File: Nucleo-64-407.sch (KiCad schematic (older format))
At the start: 72 parts, among them J1 SWD, J3 USB_B_Micro, J4 Serial 0, J5 EXP1, J6 EXP2, J7 EXP3, J8 EXP4, SW1 RESET, SW2 BOOT, U1 STM32F407VETx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

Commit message: Renamed Button so it does not contain space in teh anme.
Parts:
- SW1, SW2: footprint PrntrBoardV1:Button 4x4 -> PrntrBoardV1:Button_4x4
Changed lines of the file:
@@
-EESchema Schematic File Version 4
+EESchema Schematic File Version 5
 LIBS:Nucleo-64-407-cache
 EELAYER 29 0
@@
 F 0 "SW1" H 1300 1435 50  0000 C CNN
 F 1 "RESET" H 1300 1344 50  0000 C CNN
-F 2 "PrntrBoardV1:Button 4x4" H 1300 1350 50  0001 C CNN
+F 2 "PrntrBoardV1:Button_4x4" H 1300 1350 50  0001 C CNN
 F 3 "" H 1300 1350 50  0001 C CNN
 	1    1300 1150
@@
 F 0 "SW2" H 9450 6535 50  0000 C CNN
 F 1 "BOOT" H 9450 6444 50  0000 C CNN
-F 2 "PrntrBoardV1:Button 4x4" H 9450 6450 50  0001 C CNN
+F 2 "PrntrBoardV1:Button_4x4" H 9450 6450 50  0001 C CNN
 F 3 "" H 9450 6450 50  0001 C CNN
 	1    9450 6250

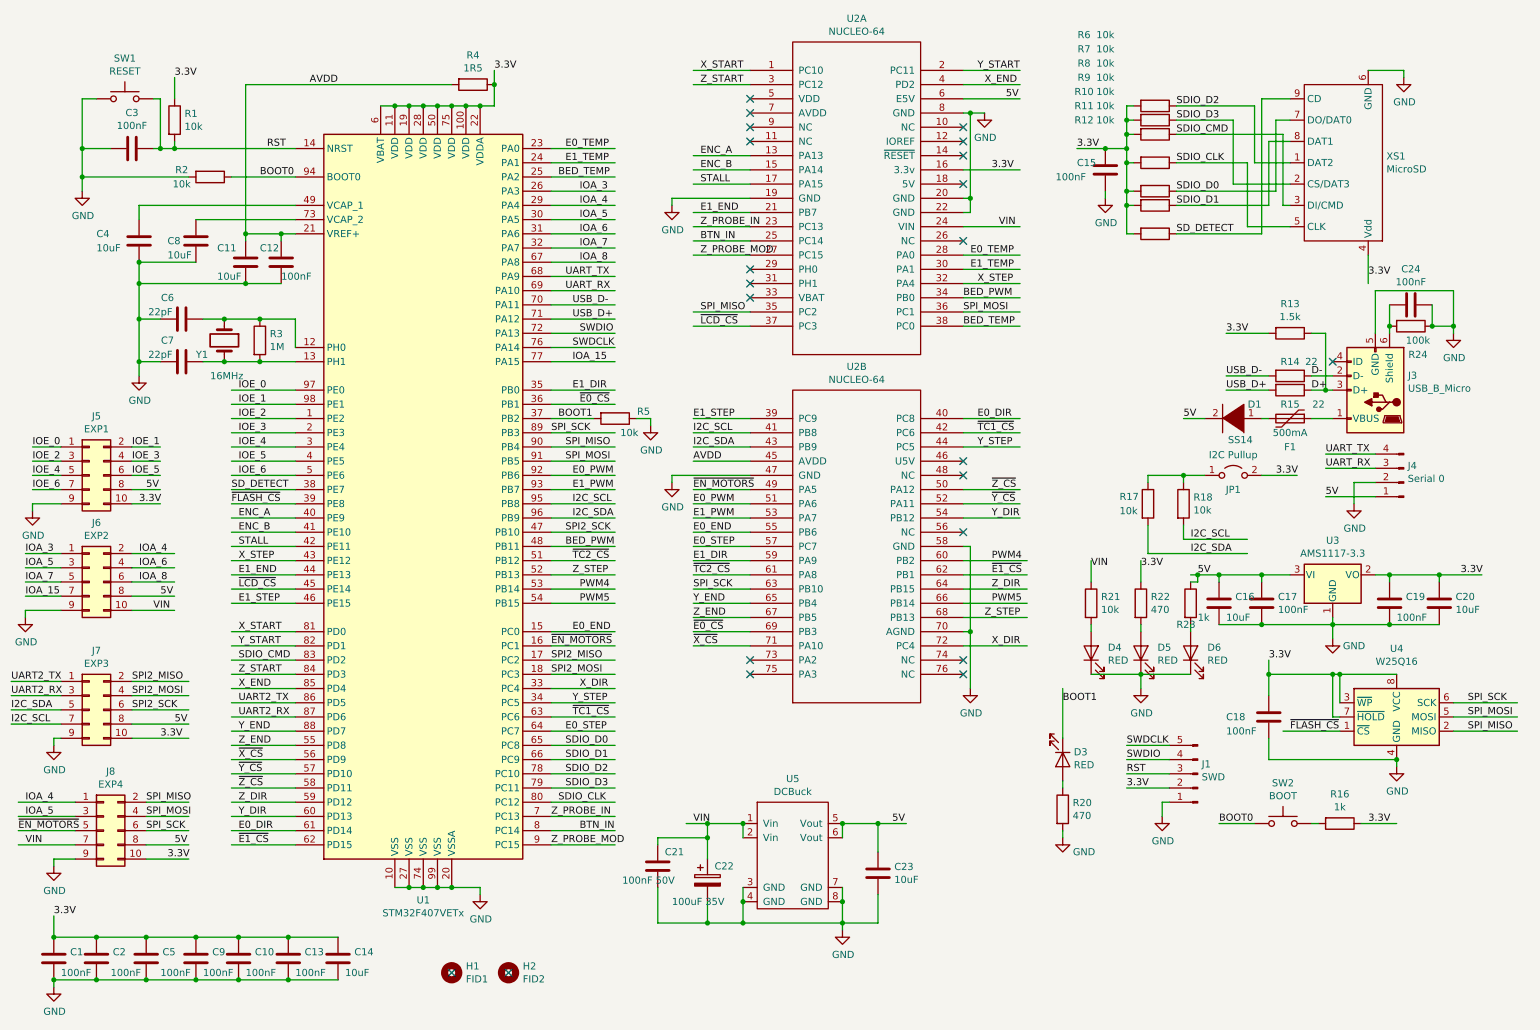
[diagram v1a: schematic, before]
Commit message: Minor updates to the nucleo-64 board. Added more signals to the extension headers. Use resistor networks. Fix diode footprint.
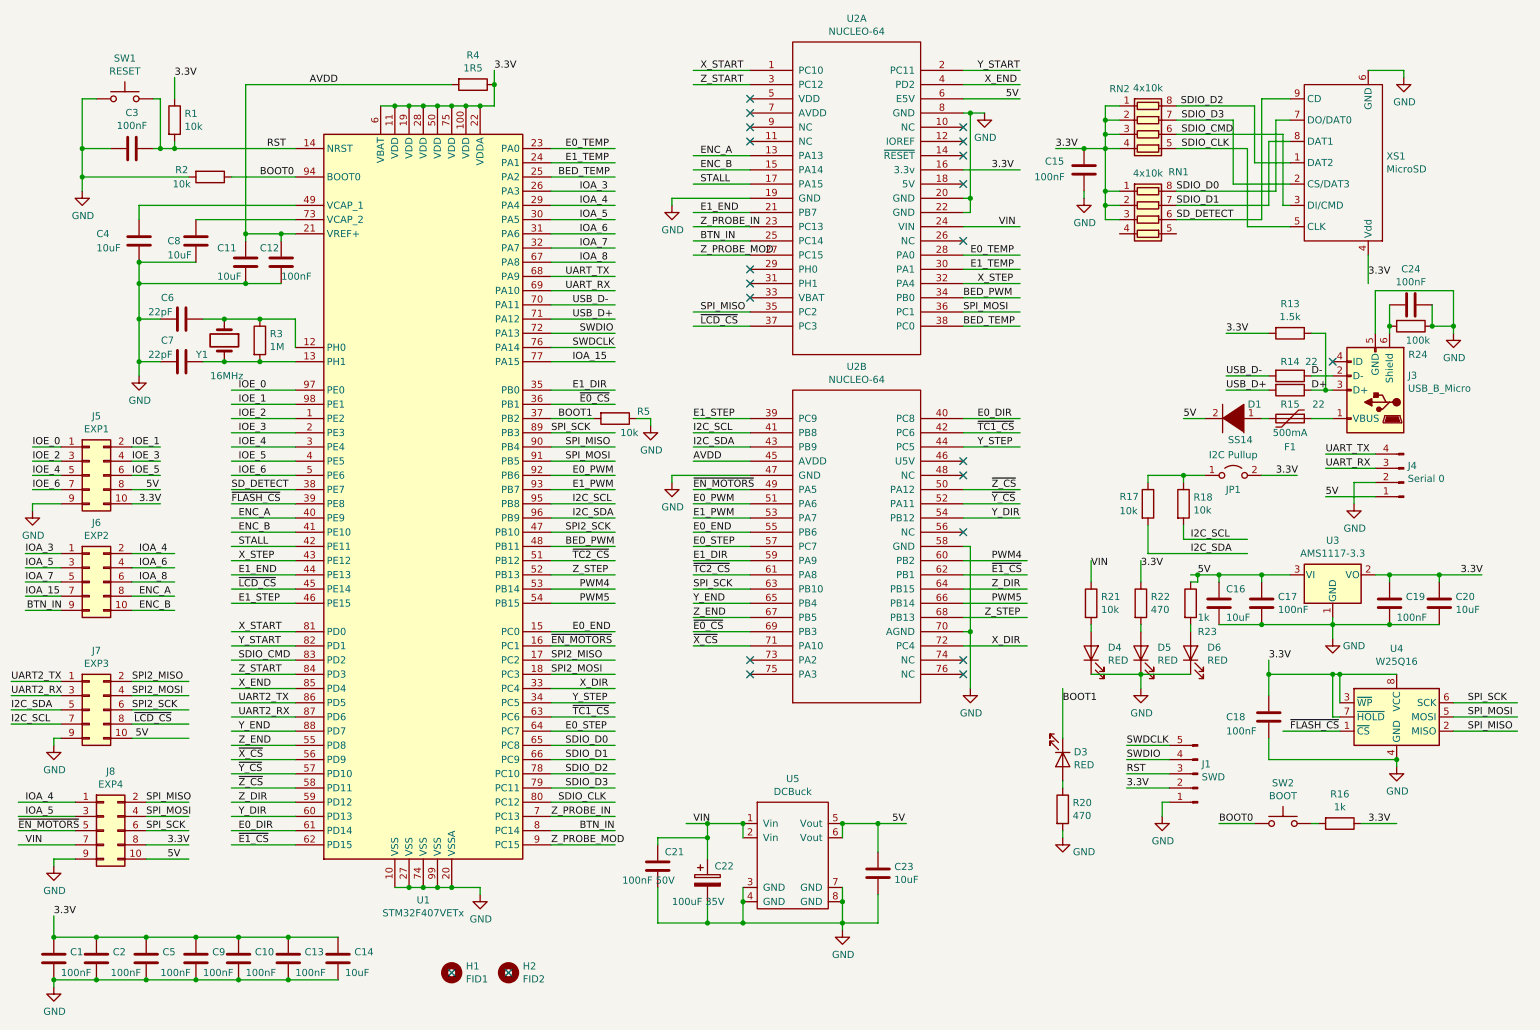
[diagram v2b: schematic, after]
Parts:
- removed R10, R11, R12, R6, R7, R8, R9: 10k, PrntrBoardV1:R_0603_1608Metric, symbol Device:R
- added RN1, RN2: 4x10k, Resistor_SMD:R_Array_Convex_4x0603, symbol Device:R_Pack04
- D1: footprint Diode_SMD:D_SOD-123F -> Diode_SMD:D_SMA
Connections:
- wire segments 410 -> 408
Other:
- moved on the sheet: C15

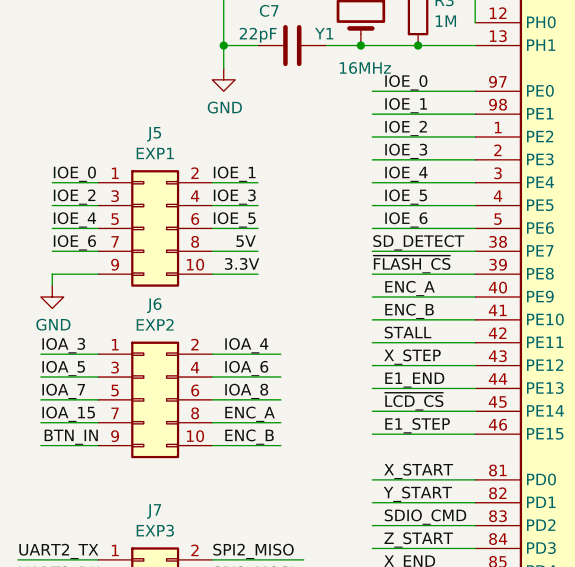
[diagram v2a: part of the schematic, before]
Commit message: Add RGB leds to IO pins.
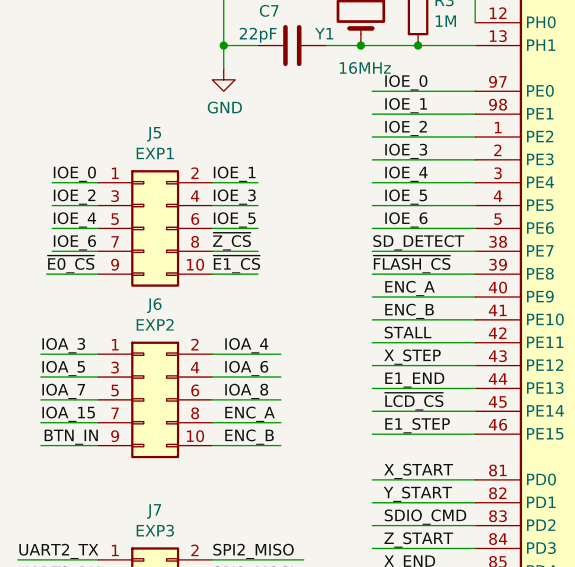
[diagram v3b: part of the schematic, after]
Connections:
- wire segments 408 -> 407
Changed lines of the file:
@@
 	850  3900 650  3900
 Wire Wire Line
-	850  4000 650  4000
-Wire Wire Line
 	1350 3600 1550 3600
 Wire Wire Line
@@
 Wire Wire Line
 	1350 3800 1550 3800
-Wire Wire Line
-	1350 3900 1550 3900
-Wire Wire Line
-	1350 4000 1550 4000
 Text Label 650  3600 0    50   ~ 0
 IOE_0
@@
 Text Label 1350 3800 0    50   ~ 0
 IOE_5
-$Comp
-L power:GND #PWR02
-U 1 1 5C6C1C05
-P 650 4050
-F 0 "#PWR02" H 650 3800 50  0001 C CNN
-F 1 "GND" H 655 3877 50  0000 C CNN
-F 2 "" H 650 4050 50  0001 C CNN
-F 3 "" H 650 4050 50  0001 C CNN
-	1    650  4050
-	1    0    0    -1
-$EndComp
-Wire Wire Line
-	650  4000 650  4050
-Text Label 1450 3900 0    50   ~ 0
-5V
-Text Label 1400 4000 0    50   ~ 0
-3.3V
 Wire Wire Line
 	850  4350 600  4350
@@
 Text Label 1375 5650 0    50   ~ 0
 5V
+Wire Wire Line
+	1350 3900 1550 3900
+Text Label 1350 3900 0    50   ~ 0
+~Z_CS
+Wire Wire Line
+	1350 4000 1550 4000
+Text Label 1350 4000 0    50   ~ 0
+~E1_CS
+Wire Wire Line
+	850  4000 625  4000
+Text Label 625  4000 0    50   ~ 0
+~E0_CS
 $EndSCHEMATC

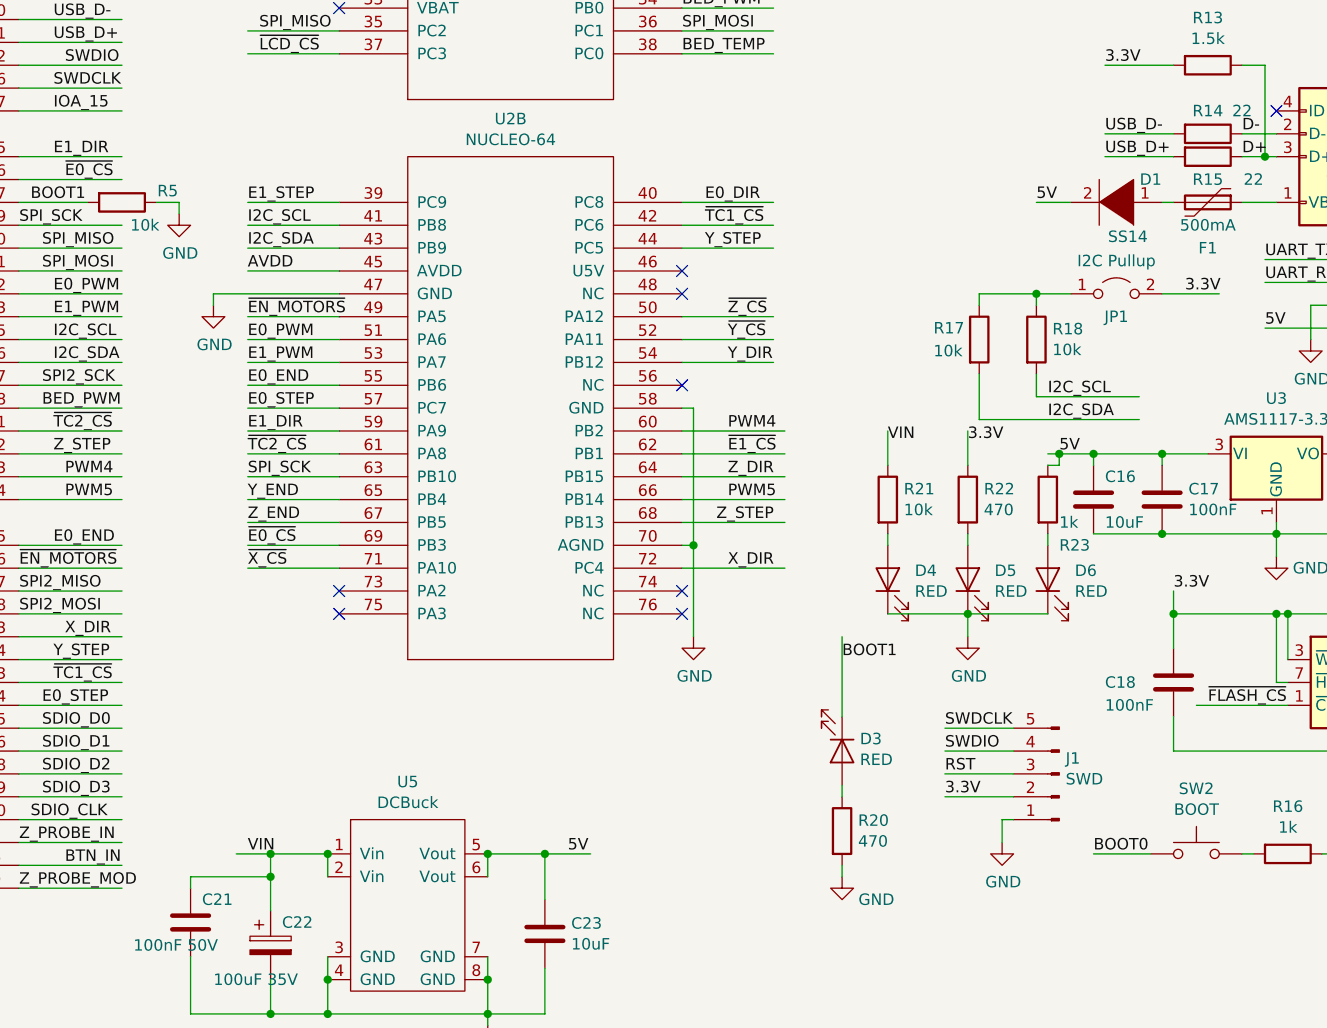
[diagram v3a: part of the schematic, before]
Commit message: Add reverse power protection to the nucleo board.
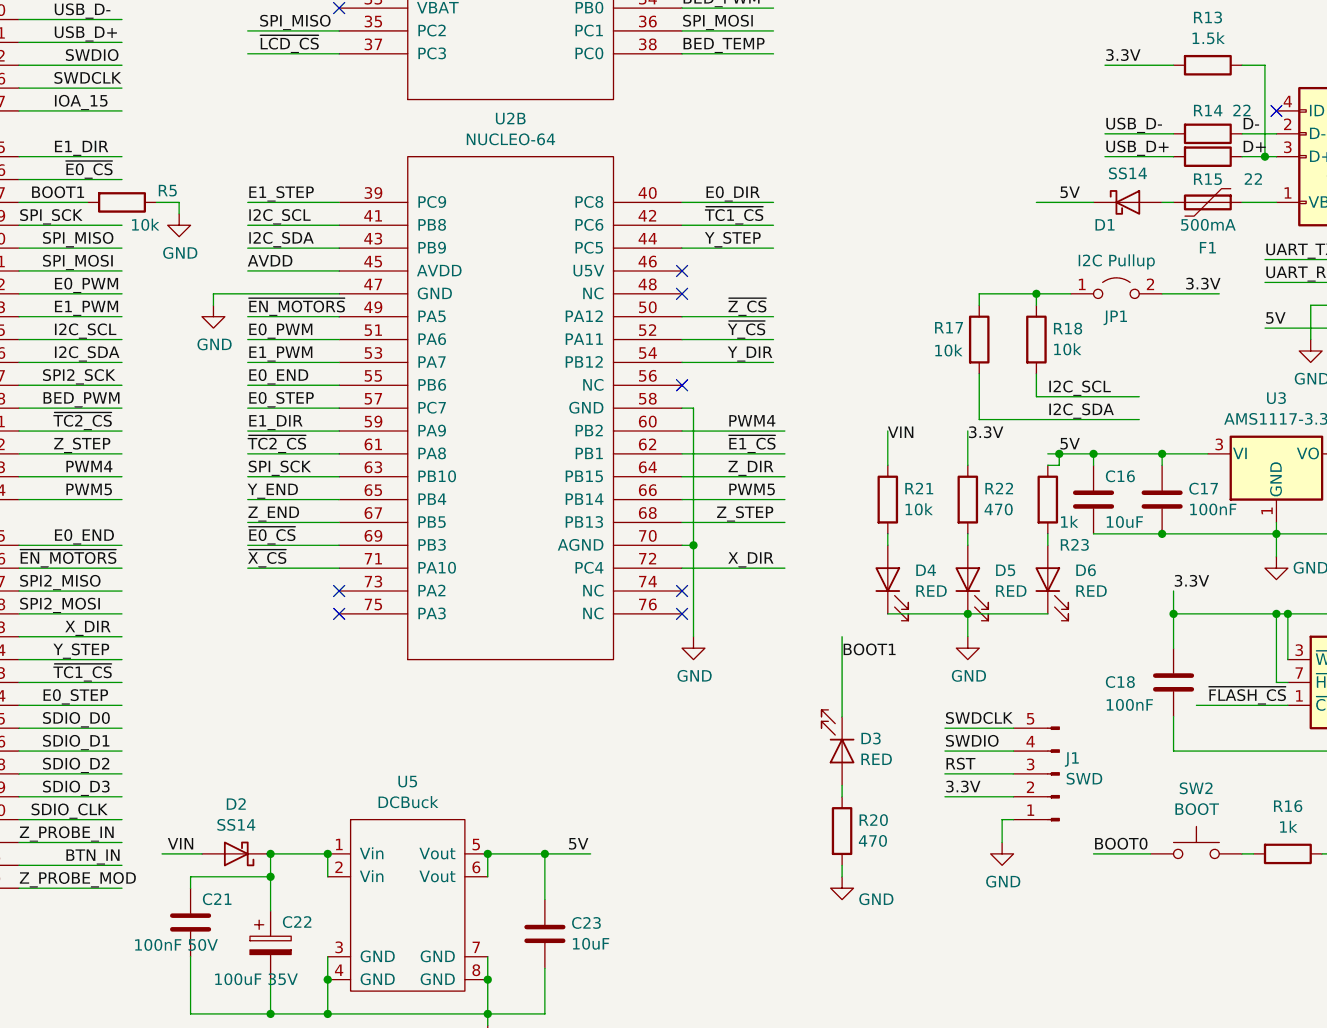
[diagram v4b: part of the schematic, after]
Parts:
- removed D1: SS14, Diode_SMD:D_SMA, symbol pspice:DIODE
- added D1, D2: SS14, Diode_SMD:D_SMA, symbol Device:D_Schottky
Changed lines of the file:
@@
 Text Label 8850 4500 0    50   ~ 0
 5V
-$Comp
-L pspice:DIODE D1
-U 1 1 5C0AF6F5
-P 9100 3400
-F 0 "D1" H 8950 3300 50  0000 C CNN
-F 1 "SS14" H 9050 3550 50  0000 C CNN
-F 2 "Diode_SMD:D_SMA" H 9100 3400 50  0001 C CNN
-F 3 "~" H 9100 3400 50  0001 C CNN
-	1    9100 3400
-	-1   0    0    1
-$EndComp
 Wire Wire Line
 	9300 3400 9350 3400
 Wire Wire Line
-	8900 3400 8750 3400
-Text Label 8750 3400 0    50   ~ 0
+	9000 3400 8750 3400
+Text Label 8850 3400 0    50   ~ 0
 5V
 $Comp
@@
 	5650 6250 5400 6250
 Connection ~ 5650 6250
-Text Label 5300 6250 0    50   ~ 0
-VIN
 $Comp
 L Device:CP C22
@@
 	1    0    0    -1
 $EndComp
-Connection ~ 5400 6250
-Wire Wire Line
-	5400 6250 5250 6250
 Connection ~ 5650 6950
 $Comp
@@
 Text Label 625  4000 0    50   ~ 0
 ~E0_CS
+$Comp
+L Device:D_Schottky D2
+U 1 1 5D6DBCCC
+P 5250 6250
+F 0 "D2" H 5250 6034 50  0000 C CNN
+F 1 "SS14" H 5250 6125 50  0000 C CNN
+F 2 "Diode_SMD:D_SMA" H 5250 6250 50  0001 C CNN
+F 3 "~" H 5250 6250 50  0001 C CNN
+	1    5250 6250
+	-1   0    0    1
+$EndComp
+Connection ~ 5400 6250
+Wire Wire Line
+	5100 6250 4925 6250
+Text Label 4950 6250 0    50   ~ 0
+VIN
+$Comp
+L Device:D_Schottky D1
+U 1 1 5D6E0286
+P 9150 3400
+F 0 "D1" H 9050 3300 50  0000 C CNN
+F 1 "SS14" H 9150 3525 50  0000 C CNN
+F 2 "Diode_SMD:D_SMA" H 9150 3400 50  0001 C CNN
+F 3 "~" H 9150 3400 50  0001 C CNN
+	1    9150 3400
+	1    0    0    -1
+$EndComp
 $EndSCHEMATC
